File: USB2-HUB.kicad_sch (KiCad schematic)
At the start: 34 parts, among them J13 IEC61076-2_M8_A-coding_01x04_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, J14 IEC61076-2_M8_A-coding_01x04_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, J15 IEC61076-2_M8_A-coding_01x04_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, J16 IEC61076-2_M8_A-coding_01x04_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, J5 USB_OTG, U4 FSUSB42MUX, U5 USB2514B-I/M2, U7 TPD4EUSB30, U8 AP22653W6, Y1 24MHz

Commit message: worked some more on converting components (unfinished)
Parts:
- removed J5: USB_OTG, CM4IO:USB_Micro-B_EDAC_UCON00686, symbol Connector:USB_OTG
- removed R7, R8: 2.2K 1%, Resistor_SMD:R_0402_1005Metric, symbol Device:R
- removed U4: FSUSB42MUX, Package_SO:MSOP-10_3x3mm_P0.5mm, symbol CM4IO:FSUSB42MX
- added C51, C52: 27pF, Capacitor_SMD:C_0402_1005Metric, symbol Device:C
- added J17: USB_OTG, symbol Connector:USB_OTG
- added R38, R39: 2.2K 1%, Resistor_SMD:R_0402_1005Metric, symbol Device:R
- added U20: FSUSB42MUX, Package_SO:MSOP-10_3x3mm_P0.5mm, symbol Interface_USB:FSUSB42MUX
- added U21: FE1.1s, Package_SO:SSOP-28_3.9x9.9mm_P0.635mm, symbol Interface_USB:FE1.1s
- added Y3: 24MHz, Crystal:Crystal_SMD_HC49-SD, symbol Device:Crystal
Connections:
- net GND: now also C51.2, C52.2, J17.5 (GND), J17.6 (Shield), R38.2, U20.10 (~{OE}), U20.5 (GND), U21.1 (VSS), U21.25 (PWRJ)
- net HD1_N: now also U21.10 (DM1)
- net HD1_P: now also U21.11 (DP1)
- net HD2_N: now also U21.8 (DM2)
- net HD2_P: now also U21.9 (DP2)
- net HD3_N: now also U21.6 (DM3)
- net HD3_P: now also U21.7 (DP3)
- net HD4_N: now also U21.4 (DM4)
- net HD4_P: now also U21.5 (DP4)
- net USB2_N: now also U20.4 (D-)
- net USB2_P: now also U20.3 (D+)
- net USBH_N: no longer U5.30 (USBDM_UP)
- net USBH_P: no longer U5.31 (USBDP_UP)
- net USBOTG: now also R38.1, R39.2, U20.2 (SEL)
- net VBUS: now also U21.18 (VBUSM)
- net nOCS1: no longer U8.4 (nFault)
- net +3.3v renamed +3.3V
- net +3.3V: now also U20.1 (VCC), U21.13 (VD33), U21.21 (VD33_O)
- net +5v renamed +5V
- net +5V: now also U21.20 (VDD5)
- new net: J17.1 (VBUS), R39.1
- new net: U20.6 (HSD1-), U21.15 (DMU)
- new net: U20.7 (HSD1+), U21.16 (DPU)
- new net: C51.1, U21.2 (XOUT), Y3.1
- new net: C52.1, U21.3 (XIN), Y3.2
- new net: J17.2 (D-), U20.8 (HSD2-)
- new net: J17.3 (D+), U20.9 (HSD2+)
- new net OVR_CUR: U21.26 (OVCJ), U8.4 (nFault)
- no-connect marks 7 -> 9
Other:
- moved on the sheet: C10, C11, C12, C13, C4, C5, C6, C7, C8, C9, R10, R11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

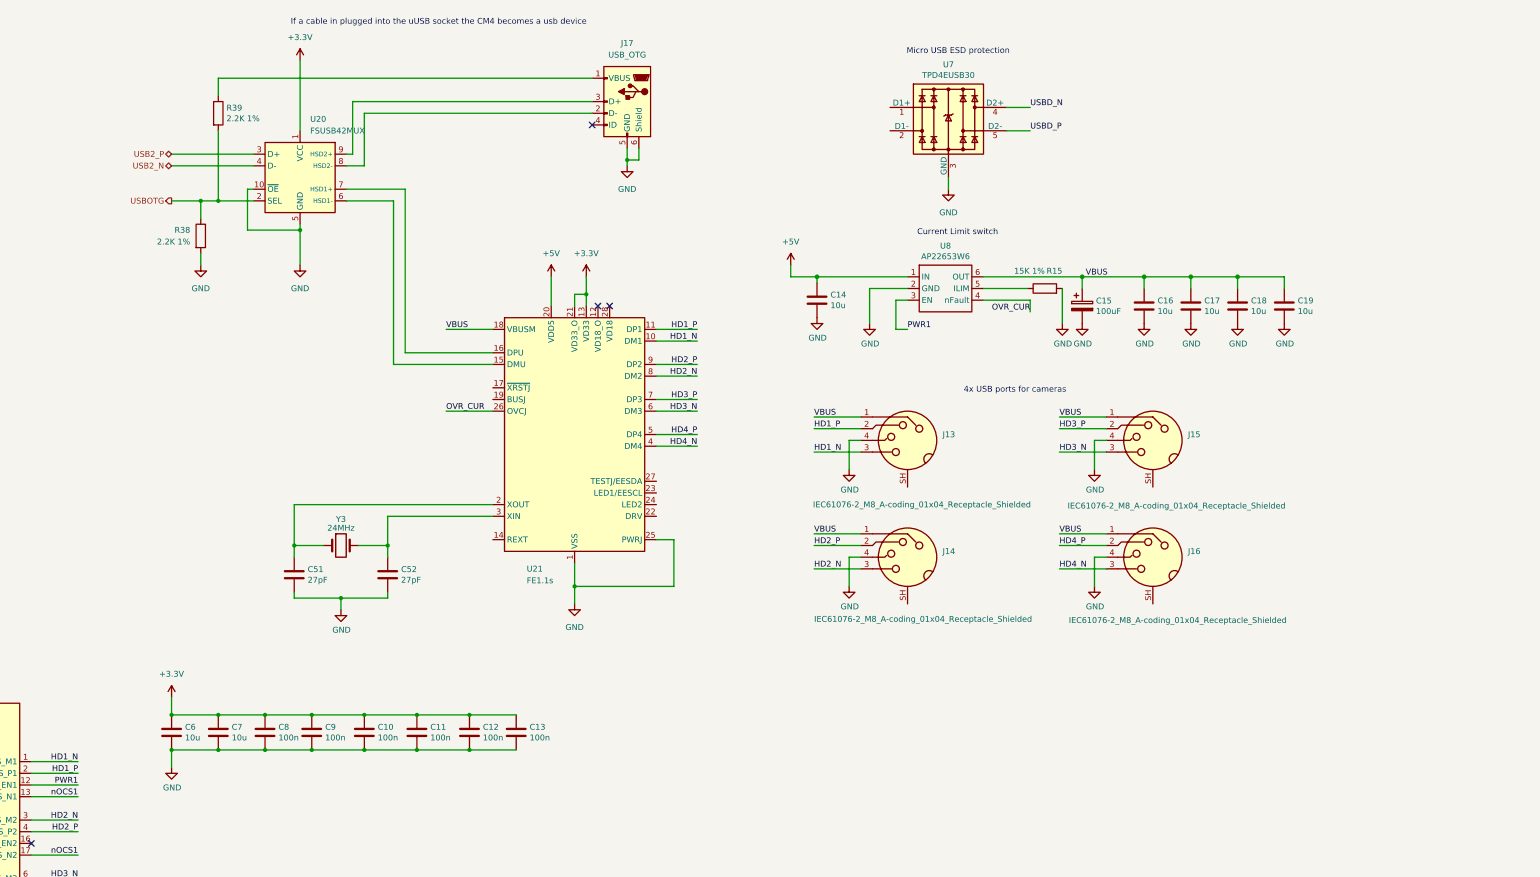
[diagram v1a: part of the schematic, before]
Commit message: power dist, hdmi, and rtc are done; finding a new usb hub
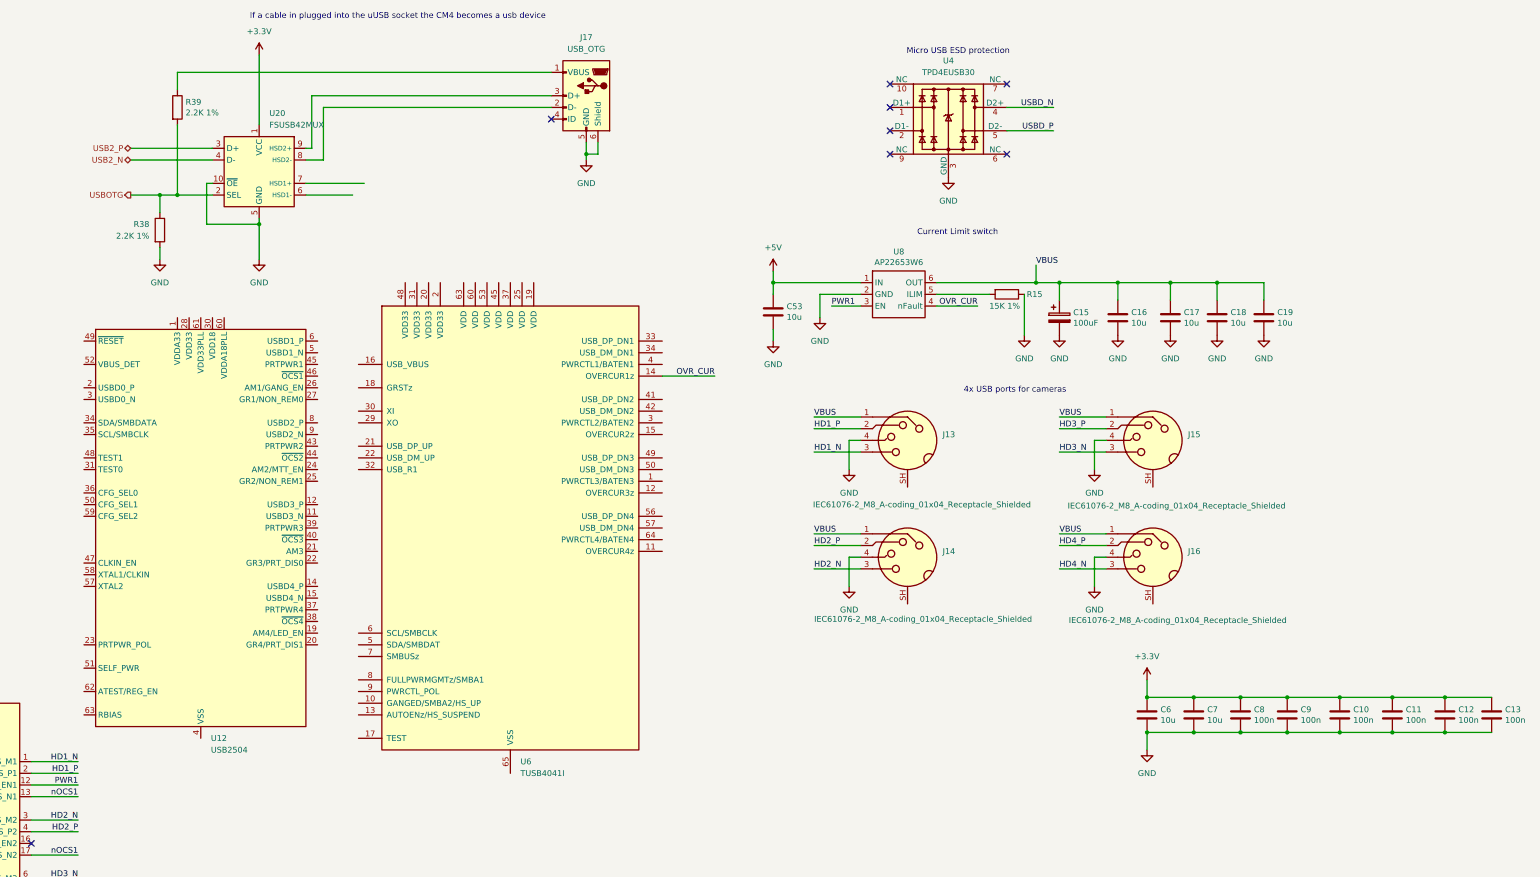
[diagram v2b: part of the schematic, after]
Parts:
- removed C14: 10u, Capacitor_SMD:C_0805_2012Metric, symbol Device:C
- removed C51, C52: 27pF, Capacitor_SMD:C_0402_1005Metric, symbol Device:C
- removed U21: FE1.1s, Package_SO:SSOP-28_3.9x9.9mm_P0.635mm, symbol Interface_USB:FE1.1s
- removed U7: TPD4EUSB30, Package_SON:USON-10_2.5x1.0mm_P0.5mm, symbol CM4IO:TPD4EUSB30
- removed Y3: 24MHz, Crystal:Crystal_SMD_HC49-SD, symbol Device:Crystal
- added C53: 10u, Capacitor_SMD:C_0805_2012Metric, symbol Device:C
- added U12: USB2504, Package_QFP:LQFP-64_10x10mm_P0.5mm, symbol Interface_USB:USB2504
- added U4: TPD4EUSB30, Package_SON:USON-10_2.5x1.0mm_P0.5mm, symbol Power_Protection:TPD4EUSB30
- added U6: TUSB4041I, Package_QFP:HTQFP-64-1EP_10x10mm_P0.5mm_EP8x8mm_Mask4.4x4.4mm_ThermalVias, symbol Interface_USB:TUSB4041I
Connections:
- net +5V: now also C53.1
- net GND: now also R15.1, C53.2, U4.3 (GND), U4.8 (GND); no longer R15.2
- net OVR_CUR: now also U6.14 (OVERCUR1z)
- net USBD_N: now also U4.4 (D2+)
- net USBD_P: now also U4.5 (D2-)
- net at U8.5 (ILIM): now also R15.2; no longer R15.1
- new net: U12.1 (VDDA33), U12.13 (VDDA33), U12.7 (VDDA33)
- new net: U12.10 (VSS), U12.16 (VSS), U12.29 (VSS), U12.4 (VSS), U12.41 (VSS), U12.53 (VSS), U12.55 (VSS), U12.64 (VSS)
- new net: U12.30 (VDD18), U12.42 (VDD18), U12.54 (VDD18)
- no-connect marks 9 -> 13
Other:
- moved on the sheet: C10, C11, C12, C13, C15, C16, C17, C18, C19, C6, C7, C8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

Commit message: made more changes
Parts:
- removed C4, C5: 27pF, Capacitor_SMD:C_0402_1005Metric, symbol Device:C
- removed R10, R11, R12, R14: 36K 1%, Resistor_SMD:R_0402_1005Metric, symbol Device:R
- removed R13: 12K 1%, Resistor_SMD:R_0402_1005Metric, symbol Device:R
- removed U12: USB2504, Package_QFP:LQFP-64_10x10mm_P0.5mm, symbol Interface_USB:USB2504
- removed U5: USB2514B-I/M2, Package_DFN_QFN:QFN-36-1EP_6x6mm_P0.5mm_EP3.7x3.7mm, symbol Interface_USB:USB2514B_Bi
- removed Y1: 24MHz, Crystal:Crystal_SMD_HC49-SD, symbol Device:Crystal
- added C26: 1 u, symbol Device:C
- added C27, C28: 27pF, Capacitor_SMD:C_0402_1005Metric, symbol Device:C
- added R19, R9: 10 k, symbol Device:R
- added R3: 9.53 k 1%, symbol Device:R
- added U12: TLV71311PDBV, Package_TO_SOT_SMD:SOT-23-5, symbol Regulator_Linear:TLV71311PDBV
- added Y3: 24MHz, Crystal:Crystal_SMD_HC49-SD, symbol Device:Crystal
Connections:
- net +3.3V is gone; now on net +3.3V_PWR: C10.1, C11.1, C12.1, C13.1, C6.1, C7.1, C8.1, C9.1, U20.1 (VCC)
- net +5V is gone; now on net +5V_PWR: C53.1, U8.1 (IN)
- net HD1_N is gone; now on net USB_1N: J13.3
- net HD1_P is gone; now on net USB_1P: J13.2
- net HD2_N is gone; now on net USB_2N: J14.3
- net HD2_P is gone; now on net USB_2P: J14.2
- net HD3_N is gone; now on net USB_3N: J15.3
- net HD3_P is gone; now on net USB_3P: J15.2
- net HD4_N is gone; now on net USB_4N: J16.3
- net HD4_P is gone; now on net USB_4P: J16.2
- net USBD_N is gone; now on net USB_Upstream_N: U4.4 (D2+)
- net USBD_P is gone; now on net USB_Upstream_P: U4.5 (D2-)
- net GND: now also J13.SH, J14.SH, J15.SH, J16.SH, U6.17 (TEST), U6.65 (VSS), U6.8 (FULLPWRMGMTz/SMBA1), C26.2, C27.2, C28.2, R3.2, U12.2 (GND)
- net OVR_CUR: now also U6.11 (OVERCUR4z), U6.12 (OVERCUR3z), U6.15 (OVERCUR2z)
- net PWR1: now also U6.4 (PWRCTL1/BATEN1)
- net USB_Upstream_N: now reaches U20.6 (HSD1-)
- net USB_Upstream_N: now also U6.22 (USB_DM_UP)
- net USB_Upstream_P: now reaches U20.7 (HSD1+)
- net USB_Upstream_P: now also U6.21 (USB_DP_UP)
- net at U6.10 (GANGED/SMBA2/HS_UP): now also U6.13 (AUTOENz/HS_SUSPEND), U6.7 (SMBUSz), U6.9 (PWRCTL_POL), R19.2
- net +5V_PWR: now reaches U6.16 (USB_VBUS)
- net +5V_PWR: now also C26.1, U12.1 (IN), U12.3 (EN)
- net at U6.18 (GRSTz): now also R9.2
- net at U6.19 (VDD): now also U6.25 (VDD), U6.37 (VDD), U6.45 (VDD), U6.53 (VDD), U6.60 (VDD), U6.63 (VDD), U12.5 (OUT)
- net +3.3V_PWR: now reaches U6.2 (VDD33)
- net +3.3V_PWR: now also U6.20 (VDD33), U6.31 (VDD33), U6.48 (VDD33), R19.1, R9.1
- net at U6.32 (USB_R1): now also R3.1
- net USB_1P: now reaches U6.33 (USB_DP_DN1)
- net USB_1N: now reaches U6.34 (USB_DM_DN1)
- net USB_2P: now reaches U6.41 (USB_DP_DN2)
- net USB_2N: now reaches U6.42 (USB_DM_DN2)
- net USB_3P: now reaches U6.49 (USB_DP_DN3)
- net USB_3N: now reaches U6.50 (USB_DM_DN3)
- net USB_4P: now reaches U6.56 (USB_DP_DN4)
- net USB_4N: now reaches U6.57 (USB_DM_DN4)
- new net: C27.1, Y3.1
- new net: C28.1, Y3.2
- no-connect marks 13 -> 12
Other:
- note removed: "USB 2.0 Hub"
- moved on the sheet: C10, C11, C12, C13, C6, C7, C8, C9, J17, R39, U4

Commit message: finished USB i think, working on general gpio in more detail
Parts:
- removed C10, C11, C12, C13, C8, C9: 100n, Capacitor_SMD:C_0402_1005Metric, symbol Device:C
- removed C15: 100uF, Capacitor_Tantalum_SMD:CP_EIA-7343-31_Kemet-D, symbol Device:CP
- removed C16, C17, C18, C19, C53, C6, C7: 10u, Capacitor_SMD:C_0805_2012Metric, symbol Device:C
- removed J13, J14, J15, J16: IEC61076-2_M8_A-coding_01x04_Receptacle_Shielded, symbol Connector:IEC61076-2_M8_A-coding_01x04_Receptacle_Shielded
- removed R15: 15K 1%, Resistor_SMD:R_0402_1005Metric, symbol Device:R
- removed U8: AP22653W6, Package_TO_SOT_SMD:SOT-23-6, symbol CM4IO:AP2553W6
- added C4: 100 n, symbol Device:C
- added R10: 90.9k 1%, symbol Device:R
- added R11: 10k 1%, symbol Device:R
- added R12, R13, R14, R21, R22, R23: 4.7k, symbol Device:R
- R3: value 9.53 k 1% -> 9.53k 1%
- R9: value 10 k -> 10k 1%
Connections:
- net +3.3V_PWR: now also R14.1, R21.1, R22.1, R23.1
- net +5V_PWR: now also R10.1; no longer U6.16 (USB_VBUS)
- net GND: now also R38.1, C4.2, R11.2, R12.2, R13.2; no longer R38.2, U6.8 (FULLPWRMGMTz/SMBA1)
- net USBOTG: now also R38.2; no longer R38.1
- net at C27.1, Y3.1: now also U6.30 (XI)
- net at C28.1, Y3.2: now also U6.29 (XO)
- net at R19.2, U6.13 (AUTOENz/HS_SUSPEND), U6.7 (SMBUSz)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: no longer U6.10 (GANGED/SMBA2/HS_UP)
- net 1.1_PWR: now reaches U12.5 (OUT), U6.19 (VDD), U6.25 (VDD), U6.37 (VDD), U6.45 (VDD), U6.53 (VDD), U6.60 (VDD), U6.63 (VDD)
- net 1.1_PWR: now also C4.1
- net USB_Ports/EN3: now reaches U6.1 (PWRCTL3/BATEN3)
- net USB_Ports/EN3: now also R22.2
- net USB_Ports/EN2: now reaches U6.3 (PWRCTL2/BATEN2)
- net USB_Ports/EN2: now also R21.2
- net USB_Ports/EN4: now reaches U6.64 (PWRCTL4/BATEN4)
- net USB_Ports/EN4: now also R23.2
- removed net OVR_CUR: U6.11 (OVERCUR4z), U6.12 (OVERCUR3z), U6.14 (OVERCUR1z), U6.15 (OVERCUR2z)
- net PWR1 renamed USB_Ports/EN1
- net USB_Ports/EN1: now also R14.2
- net USB_1N renamed USB_Ports/USB_1N
- net USB_1P renamed USB_Ports/USB_1P
- net USB_2N renamed USB_Ports/USB_2N
- net USB_2P renamed USB_Ports/USB_2P
- net USB_3N renamed USB_Ports/USB_3N
- net USB_3P renamed USB_Ports/USB_3P
- net USB_4N renamed USB_Ports/USB_4N
- net USB_4P renamed USB_Ports/USB_4P
- new net: R10.2, R11.1, U6.16 (USB_VBUS)
- new net: R12.1, U6.8 (FULLPWRMGMTz/SMBA1)
- new net: R13.1, U6.10 (GANGED/SMBA2/HS_UP)
- new net USB_Ports/OC1: U6.14 (OVERCUR1z)
- new net USB_Ports/OC2: U6.15 (OVERCUR2z)
- new net USB_Ports/OC3: U6.12 (OVERCUR3z)
- new net USB_Ports/OC4: U6.11 (OVERCUR4z)
- no-connect marks 12 -> 9
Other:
- added sheet USB_Ports (USB_Ports.kicad_sch)
- note added: "If a cable in plugged into the microUSB socket the CM4 becomes a usb device"
- note removed: "4x USB ports for cameras"
- note removed: "Current Limit switch"
- note removed: "If a cable in plugged into the uUSB socket the CM4 becomes a usb device"
- moved on the sheet: C26, C27, C28, R19, R3, R38, R9, U12, U4, U6, Y3

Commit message: we ballin??
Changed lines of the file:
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@@
 	)
 	(junction
-		(at 106.68 175.26)
-		(diameter 0)
-		(color 0 0 0 0)
-	)
-	(junction
 		(at 52.07 109.22)
 		(diameter 1.016)
@@
 	)
 	(junction
-		(at 106.68 177.8)
-		(diameter 0)
-		(color 0 0 0 0)
-	)
-	(junction
 		(at 104.14 162.56)
 		(diameter 0)
@@
 	)
 	(junction
+		(at 88.9 179.07)
+		(diameter 0)
+		(color 0 0 0 0)
+	)
+	(junction
 		(at 139.7 71.12)
 		(diameter 0)
@@
 	(wire
 		(pts
-			(xy 88.9 173.99) (xy 88.9 177.8)
+			(xy 88.9 173.99) (xy 88.9 179.07)
 		)
 		(stroke
@@
 	(wire
 		(pts
+			(xy 88.9 179.07) (xy 97.79 179.07)
+		)
+		(stroke
+			(width 0)
+			(type default)
+		)
+	)
+	(wire
+		(pts
 			(xy 39.37 63.5) (xy 50.8 63.5)
 		)
@@
 	(wire
 		(pts
-			(xy 97.79 175.26) (xy 106.68 175.26)
-		)
-		(stroke
-			(width 0)
-			(type default)
-		)
-	)
-	(wire
-		(pts
 			(xy 88.9 53.34) (xy 88.9 54.61)
 		)
@@
 	(wire
 		(pts
-			(xy 88.9 177.8) (xy 106.68 177.8)
-		)
-		(stroke
-			(width 0)
-			(type default)
-		)
-	)
-	(wire
-		(pts
 			(xy 104.14 167.64) (xy 109.22 167.64)
 		)
@@
 	(wire
 		(pts
-			(xy 106.68 172.72) (xy 106.68 175.26)
+			(xy 106.68 172.72) (xy 106.68 182.88)
 		)
 		(stroke
@@
 	(wire
 		(pts
-			(xy 106.68 177.8) (xy 106.68 182.88)
-		)
-		(stroke
-			(width 0)
-			(type default)
-		)
-	)
-	(wire
-		(pts
 			(xy 240.03 26.67) (xy 240.03 27.94)
 		)
@@
 	(wire
 		(pts
-			(xy 97.79 173.99) (xy 97.79 175.26)
+			(xy 97.79 173.99) (xy 97.79 179.07)
 		)
 		(stroke
@@
 	(wire
 		(pts
-			(xy 72.39 109.22) (xy 72.39 104.14)
+			(xy 88.9 179.07) (xy 88.9 185.42)
 		)
 		(stroke
 			(width 0)
-			(type solid)
+			(type default)
 		)
 	)
 	(wire
 		(pts
-			(xy 50.8 24.13) (xy 50.8 41.91)
+			(xy 72.39 109.22) (xy 72.39 104.14)
 		)
 		(stroke
 			(width 0)
-			(type default)
+			(type solid)
 		)
 	)
 	(wire
 		(pts
-			(xy 242.57 44.45) (xy 250.19 44.45)
+			(xy 50.8 24.13) (xy 50.8 41.91)
 		)
 		(stroke
@@
 	(wire
 		(pts
-			(xy 104.14 162.56) (xy 104.14 167.64)
+			(xy 242.57 44.45) (xy 250.19 44.45)
 		)
 		(stroke
@@
 	(wire
 		(pts
-			(xy 132.08 71.12) (xy 132.08 73.66)
+			(xy 104.14 162.56) (xy 104.14 167.64)
 		)
 		(stroke
@@
 	(wire
 		(pts
-			(xy 106.68 175.26) (xy 106.68 177.8)
+			(xy 132.08 71.12) (xy 132.08 73.66)
 		)
 		(stroke
@@
 	)
 	(symbol
+		(lib_name "GND_4")
+		(lib_id "power:GND")
+		(at 88.9 185.42 0)
+		(unit 1)
+		(exclude_from_sim no)
+		(in_bom yes)
+		(on_board yes)
+		(dnp no)
+		(fields_autoplaced yes)
+		(property "Reference" "#PWR055"
+			(at 88.9 191.77 0)
+			(effects
+				(font
+					(size 1.27 1.27)
+				)
+				(hide yes)
+			)
+		)
+		(property "Value" "GND"
+			(at 88.9 190.5 0)
+			(effects
+				(font
+					(size 1.27 1.27)
+				)
+			)
+		)
+		(property "Footprint" ""
+			(at 88.9 185.42 0)
+			(effects
+				(font
+					(size 1.27 1.27)
+				)
+				(hide yes)
+			)
+		)
+		(property "Datasheet" ""
+			(at 88.9 185.42 0)
+			(effects
+				(font
+					(size 1.27 1.27)
+				)
+				(hide yes)
+			)
+		)
+		(property "Description" "Power symbol creates a global label with name \"GND\" , ground"
+			(at 88.9 185.42 0)
+			(effects
+				(font
+					(size 1.27 1.27)
+				)
+				(hide yes)
+			)
+		)
+		(pin "1"
+		)
+		(instances
+			(project "PiBoard"
+				(path "/e4d65698-b8ec-4bf6-9f2b-a5010377155a/ba481c31-e70b-40cd-84a6-4c7235d9d730"
+					(reference "#PWR055")
+					(unit 1)
+				)
+			)
+		)
+	)
+	(symbol
 		(lib_id "Device:R")
 		(at 105.41 119.38 0)
@@
 			)
 		)
-		(property "Description" ""
+		(property "Description" "Two pin crystal"
 			(at 62.23 109.22 0)
 			(effects
@@
 	)
 	(symbol
-		(lib_name "USB_OTG_1")
 		(lib_id "Connector:USB_OTG")
 		(at 88.9 39.37 0)
